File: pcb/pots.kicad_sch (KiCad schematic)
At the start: 9 parts, among them SW1 DSHP03TSGET

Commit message: CI/CD Changes
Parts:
- RV1, RV2, RV3, RV4, RV5, RV6, RV7, RV8: Spice_Lib_File SPICE models/pot.lib -> (none); Spice_Model Potentiometer -> (none); Spice_Netlist_Enabled Y -> (none); Spice_Primitive X -> (none)

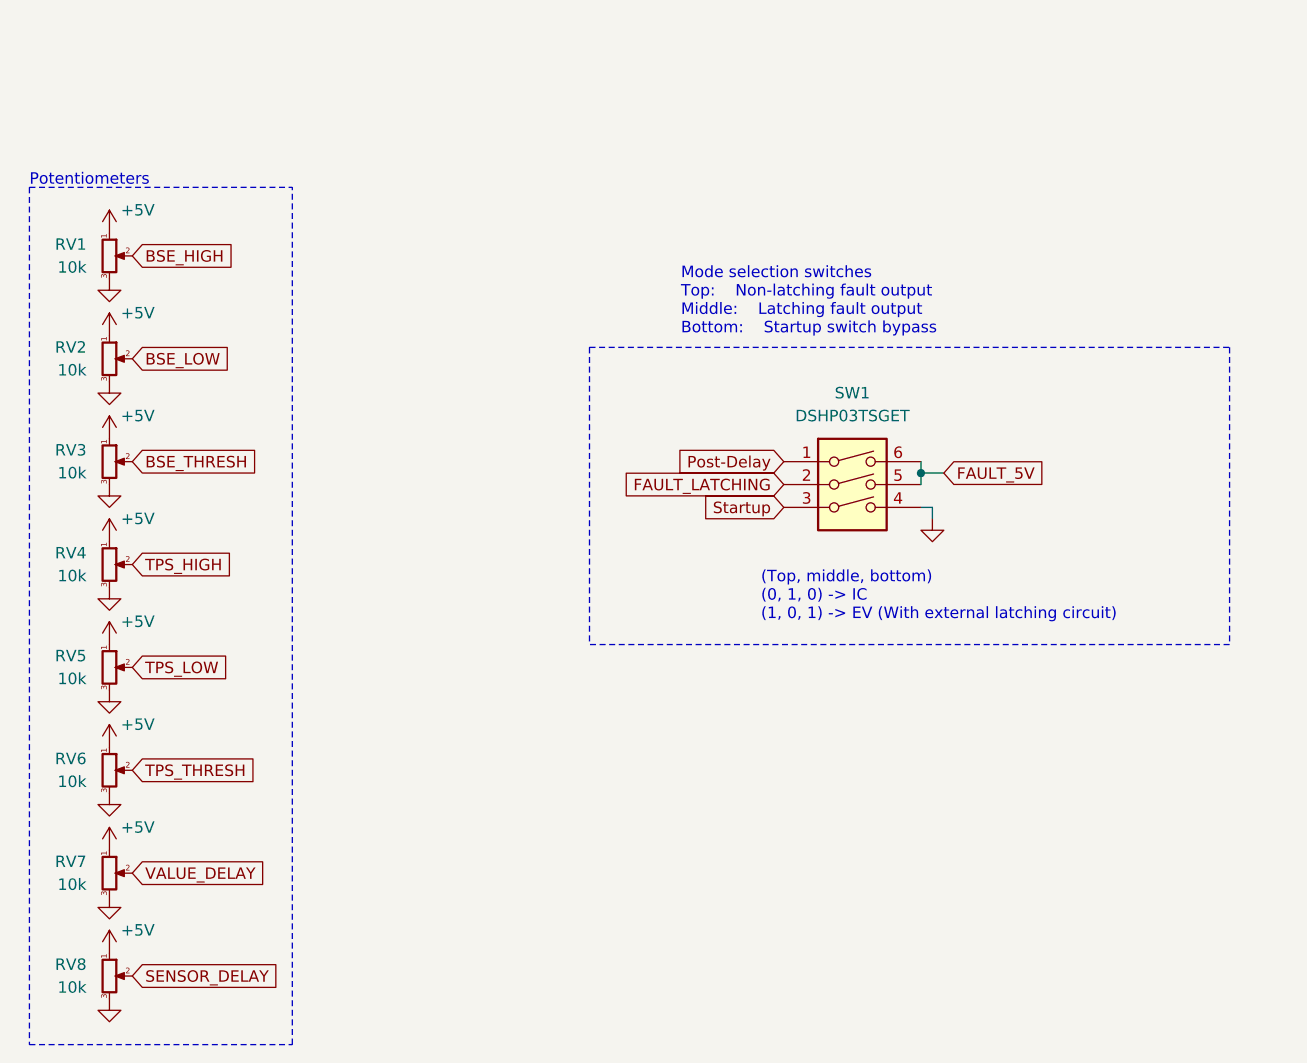
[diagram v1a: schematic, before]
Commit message: Initial Schematic and PCB changes for BR2025
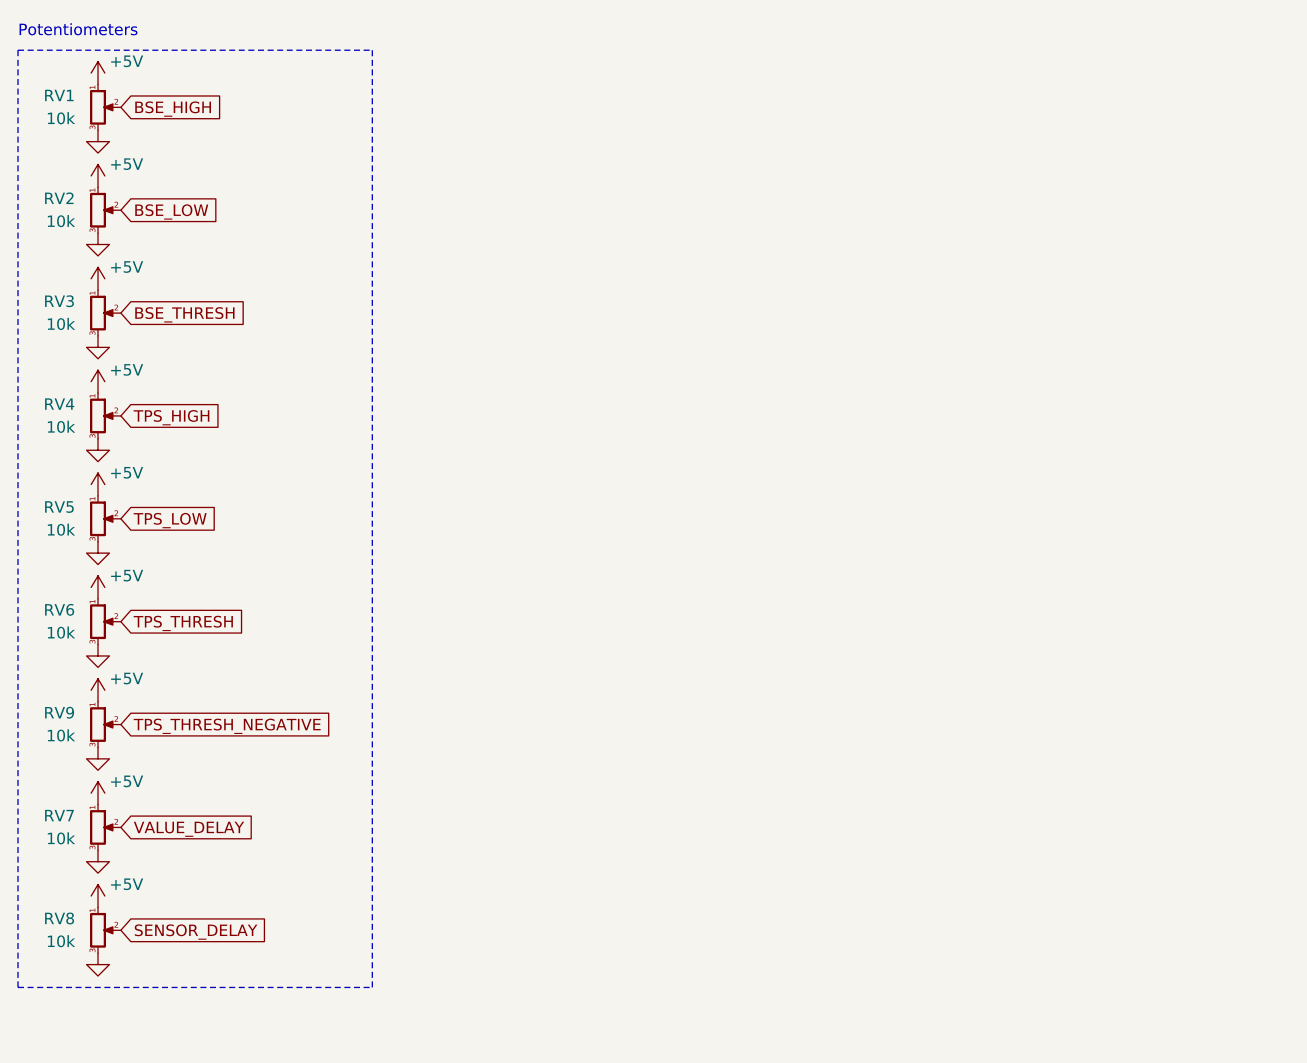
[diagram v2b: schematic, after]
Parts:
- removed SW1: DSHP03TSGET, Button_Switch_SMD:SW_DIP_SPSTx03_Slide_KingTek_DSHP03TS_W7.62mm_P1.27mm, symbol Switch:SW_DIP_x03
- added RV9: 10k, Potentiometer_SMD:Potentiometer_Bourns_TC33X_Vertical, symbol Device:R_Potentiometer_Small
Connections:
- net +5V: now also RV9.1
- net GND: now also RV9.3
- new net TPS_THRESH_NEGATIVE: RV9.2
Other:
- note removed: "(Top, middle, bottom) (0, 1, 0) -> IC (1, 0, 1) -> EV (With external latching circuit)"
- note removed: "Mode selection switches Top: Non-latching fault output Middle: Latching fault output Bottom: Startup switch bypass"
- moved on the sheet: RV1, RV2, RV3, RV4, RV5, RV6, RV7, RV8
